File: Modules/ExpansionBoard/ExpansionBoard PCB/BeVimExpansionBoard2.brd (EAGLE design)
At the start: 78.4 x 82.5 mm, 19 parts, among them IC3 4051N, IC4 4015N, U1 OPAMP

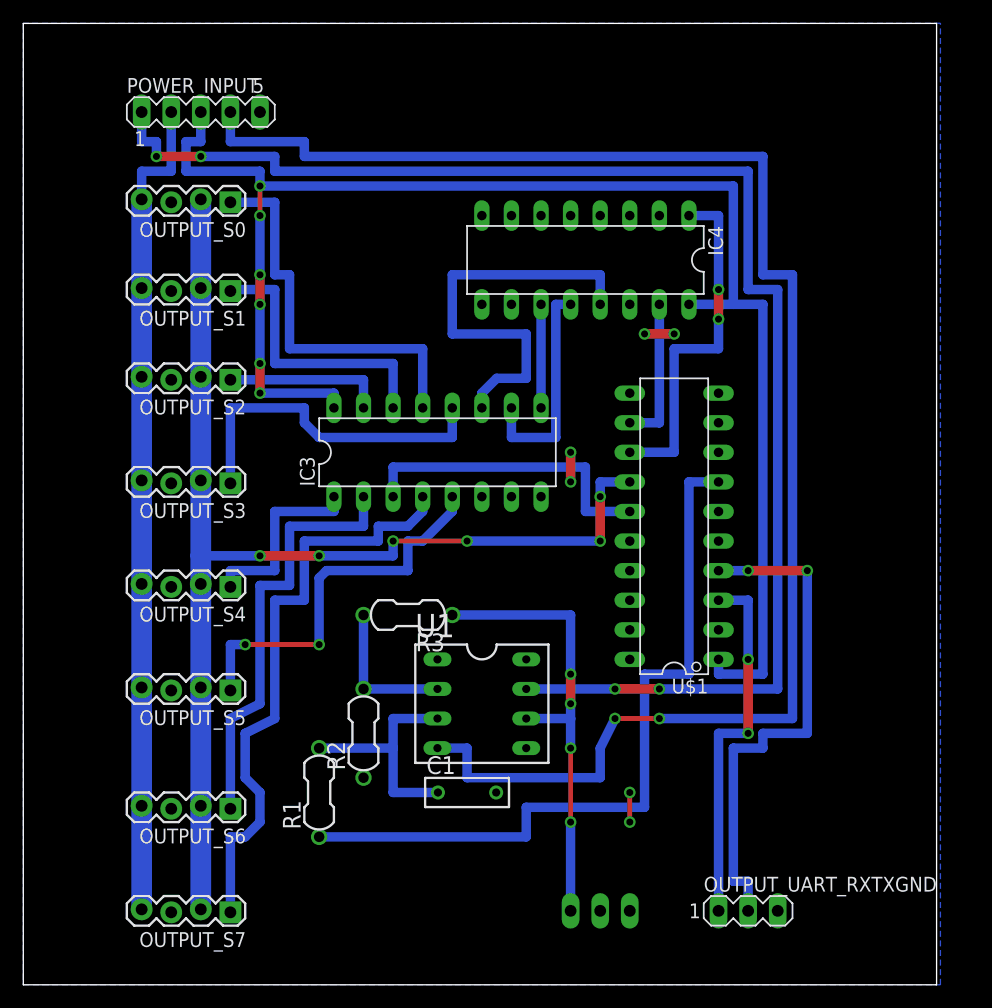
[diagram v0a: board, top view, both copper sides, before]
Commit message: Atualização da placa de controle para ter entrada para a placa de expansao
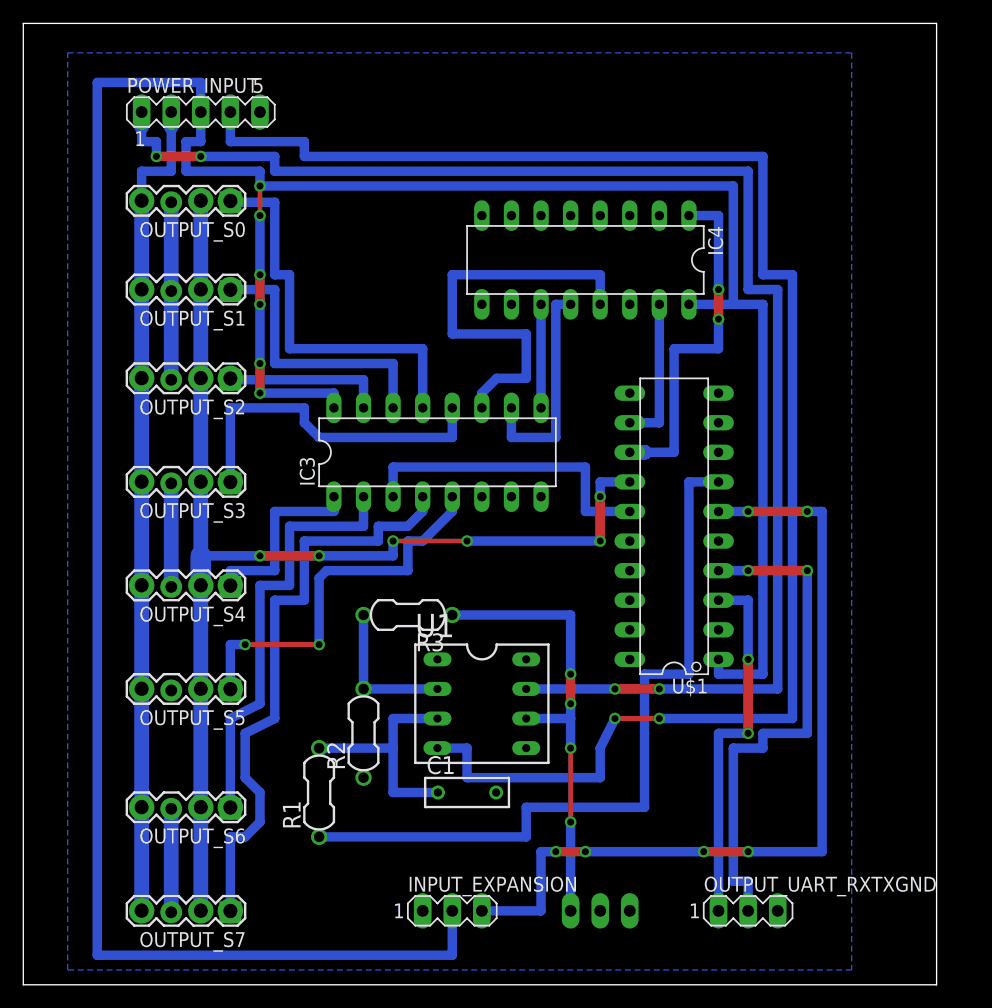
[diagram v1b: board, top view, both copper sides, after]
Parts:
- added INPUT_EXPANSION: (no value), con-lstb:MA03-1
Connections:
- new net INPUT_EXP: INPUT_EXPANSION.3, U$1.6
- net +3: now also INPUT_EXPANSION.2
- net GND: now also INPUT_EXPANSION.1
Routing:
- net +3: track 133.3 -> 254.0 mm
- net INPUT_EXP: track 0.00 -> 72.4 mm, vias 0 -> 6
- net GND: track 8.04 -> 33.1 mm, vias 6 -> 0
- net CLK: track 29.2 -> 30.5 mm
- net +12: track 124.5 -> 125.7 mm
- net +5: track 70.0 -> 71.0 mm, vias 0 -> 7
- net SDA_S7: track 51.4 -> 51.5 mm, vias 0 -> 1
- net SDA_S4: track 16.5 -> 16.6 mm, vias 0 -> 1
- net SDA_S3: track 29.7 -> 29.9 mm, vias 0 -> 1
- net SDA_S1: track 24.1 -> 24.3 mm, vias 0 -> 1
- net SDA_S6: vias 0 -> 1
- net SDA_S5: vias 2 -> 3
- net SDA_S0: vias 0 -> 1
- net SCL: vias 6 -> 14
